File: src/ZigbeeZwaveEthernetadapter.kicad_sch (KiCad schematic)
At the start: 19 parts, among them J1 Barrel_Jack, J11 Conn_02x06_Odd_Even, J12 Conn_01x06, J14 Conn_01x06, J2 USB_B_Micro, J3 USB4125-GF-A, J31 Conn_02x05_Odd_Even, U1 TLV1117-33

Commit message: Add: BOM_A.pdf
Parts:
- J11: Manufacturer Part No. - -> RS2-12-G; Vendor - -> Digikey; Vendor Part No. - -> 2057-RS2-12-G-ND
- J12: Manufacturer Part No. - -> RS1-06-G; Vendor - -> Digikey; Vendor Part No. - -> 2057-RS1-06-G-ND
- J31: Manufacturer Part No. - -> RS2-10-G; Vendor - -> Digikey; Vendor Part No. - -> 2057-RS2-10-G-ND
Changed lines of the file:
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@@
       (effects (font (size 1.27 1.27)) hide)
     )
-    (property "Manufacturer Part No." "-" (at 62.23 48.26 0)
-      (effects (font (size 1.27 1.27)) hide)
-    )
-    (property "Vendor" "-" (at 62.23 48.26 0)
-      (effects (font (size 1.27 1.27)) hide)
-    )
-    (property "Vendor Part No." "-" (at 62.23 48.26 0)
+    (property "Manufacturer Part No." "RS2-12-G" (at 62.23 48.26 0)
+      (effects (font (size 1.27 1.27)) hide)
+    )
+    (property "Vendor" "Digikey" (at 62.23 48.26 0)
+      (effects (font (size 1.27 1.27)) hide)
+    )
+    (property "Vendor Part No." "2057-RS2-12-G-ND" (at 62.23 48.26 0)
       (effects (font (size 1.27 1.27)) hide)
     )
@@
       (effects (font (size 1.27 1.27)) hide)
     )
-    (property "Manufacturer Part No." "-" (at 151.13 63.5 0)
-      (effects (font (size 1.27 1.27)) hide)
-    )
-    (property "Vendor" "-" (at 151.13 63.5 0)
-      (effects (font (size 1.27 1.27)) hide)
-    )
-    (property "Vendor Part No." "-" (at 151.13 63.5 0)
+    (property "Manufacturer Part No." "RS2-10-G" (at 151.13 63.5 0)
+      (effects (font (size 1.27 1.27)) hide)
+    )
+    (property "Vendor" "Digikey" (at 151.13 63.5 0)
+      (effects (font (size 1.27 1.27)) hide)
+    )
+    (property "Vendor Part No." "2057-RS2-10-G-ND" (at 151.13 63.5 0)
       (effects (font (size 1.27 1.27)) hide)
     )
@@
       (effects (font (size 1.27 1.27)) hide)
     )
-    (property "Manufacturer Part No." "-" (at 52.07 93.98 0)
-      (effects (font (size 1.27 1.27)) hide)
-    )
-    (property "Vendor" "-" (at 52.07 93.98 0)
-      (effects (font (size 1.27 1.27)) hide)
-    )
-    (property "Vendor Part No." "-" (at 52.07 93.98 0)
-      (effects (font (size 1.27 1.27)) hide)
-    )
+    (property "Manufacturer Part No." "RS1-06-G" (at 52.07 93.98 0)
+      (effects (font (size 1.27 1.27)) hide)
+    )
+    (property "Vendor" "Digikey" (at 52.07 93.98 0)
+      (effects (font (size 1.27 1.27)) hide)
+    )
+    (property "Vendor Part No." "2057-RS1-06-G-ND" (at 52.07 93.98 0)
+      (effects (font (size 1.27 1.27)) hide)
+    )

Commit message: Mod: Schematic and PCB-Layout, finished new Version.
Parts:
- added H101, H102, H103, H104: MountingHole, MountingHole:MountingHole_2.7mm_M2.5_DIN965, symbol Mechanical:MountingHole
- added H105, H106, H107, H108: MountingHole, MountingHole:MountingHole_3.2mm_M3_DIN965, symbol Mechanical:MountingHole
- J14: Manufacturer Part No. - -> RS1-06-G; Vendor - -> Digikey; Vendor Part No. - -> 2057-RS1-06-G-ND
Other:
- note added: "Only one plug can be used at a time!"
- note added: "PCB Holes"
- note added: "WIZ Holes"
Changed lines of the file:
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@@
     (effects (font (size 1.27 1.27)) (justify right bottom))
+  )
+  (text "Only one plug can be used at a time!" (at 266.7 127 90)
+    (effects (font (size 2.54 2.54) (thickness 1.016) bold) (justify left bottom))
   )
   (text "WIZ ISP / Debug\nConnector" (at 49.53 76.2 0)
@@
   )
   (text "Raspberry Pi\nConnector" (at 139.7 38.1 0)
+    (effects (font (size 1.27 1.27) (thickness 0.254) bold) (justify left bottom))
+  )
+  (text "WIZ Holes" (at 49.53 172.72 0)
+    (effects (font (size 1.27 1.27) (thickness 0.254) bold) (justify left bottom))
+  )
+  (text "PCB Holes" (at 125.73 172.72 0)
     (effects (font (size 1.27 1.27) (thickness 0.254) bold) (justify left bottom))
   )
@@
     )
   )
+  (symbol (lib_id "Mechanical:MountingHole") (at 152.4 177.8 0) (unit 1)
+    (in_bom yes) (on_board yes) (dnp no) (fields_autoplaced)
+    (property "Reference" "H106" (at 154.94 176.53 0)
+      (effects (font (size 1.27 1.27)) (justify left))
+    )
+    (property "Value" "MountingHole" (at 154.94 179.07 0)
+      (effects (font (size 1.27 1.27)) (justify left))
+    )
+    (property "Footprint" "MountingHole:MountingHole_3.2mm_M3_DIN965" (at 152.4 177.8 0)
+      (effects (font (size 1.27 1.27)) hide)
+    )
+    (property "Datasheet" "~" (at 152.4 177.8 0)
+      (effects (font (size 1.27 1.27)) hide)
+    )
+    (instances
+      (project "ZigbeeZwaveEthernetadapter"
+        (path "/bfaac094-0365-40a4-8b7a-d4d62ace544e"
+          (reference "H106") (unit 1)
+        )
+      )
+    )
+  )
   (symbol (lib_id "Device:LED") (at 165.1 88.9 90) (unit 1)
     (in_bom yes) (on_board yes) (dnp no) (fields_autoplaced)
@@
     )
   )
+  (symbol (lib_id "Mechanical:MountingHole") (at 152.4 190.5 0) (unit 1)
+    (in_bom yes) (on_board yes) (dnp no) (fields_autoplaced)
+    (property "Reference" "H107" (at 154.94 189.23 0)
+      (effects (font (size 1.27 1.27)) (justify left))
+    )
+    (property "Value" "MountingHole" (at 154.94 191.77 0)
+      (effects (font (size 1.27 1.27)) (justify left))
+    )
+    (property "Footprint" "MountingHole:MountingHole_3.2mm_M3_DIN965" (at 152.4 190.5 0)
+      (effects (font (size 1.27 1.27)) hide)
+    )
+    (property "Datasheet" "~" (at 152.4 190.5 0)
+      (effects (font (size 1.27 1.27)) hide)
+    )
+    (instances
+      (project "ZigbeeZwaveEthernetadapter"
+        (path "/bfaac094-0365-40a4-8b7a-d4d62ace544e"
+          (reference "H107") (unit 1)
+        )
+      )
+    )
+  )
   (symbol (lib_id "power:+5V") (at 231.14 134.62 0) (unit 1)
     (in_bom yes) (on_board yes) (dnp no) (fields_autoplaced)
@@
       (effects (font (size 1.27 1.27)) hide)
     )
-    (property "Manufacturer Part No." "-" (at 52.07 144.78 0)
-      (effects (font (size 1.27 1.27)) hide)
-    )
-    (property "Vendor" "-" (at 52.07 144.78 0)
-      (effects (font (size 1.27 1.27)) hide)
-    )
-    (property "Vendor Part No." "-" (at 52.07 144.78 0)
+    (property "Manufacturer Part No." "RS1-06-G" (at 52.07 144.78 0)
+      (effects (font (size 1.27 1.27)) hide)
+    )
+    (property "Vendor" "Digikey" (at 52.07 144.78 0)
+      (effects (font (size 1.27 1.27)) hide)
+    )
+    (property "Vendor Part No." "2057-RS1-06-G-ND" (at 52.07 144.78 0)
       (effects (font (size 1.27 1.27)) hide)
     )
@@
     )
   )
+  (symbol (lib_id "Mechanical:MountingHole") (at 127 177.8 0) (unit 1)
+    (in_bom yes) (on_board yes) (dnp no) (fields_autoplaced)
+    (property "Reference" "H105" (at 129.54 176.53 0)
+      (effects (font (size 1.27 1.27)) (justify left))
+    )
+    (property "Value" "MountingHole" (at 129.54 179.07 0)
+      (effects (font (size 1.27 1.27)) (justify left))
+    )
+    (property "Footprint" "MountingHole:MountingHole_3.2mm_M3_DIN965" (at 127 177.8 0)
+      (effects (font (size 1.27 1.27)) hide)
+    )
+    (property "Datasheet" "~" (at 127 177.8 0)
+      (effects (font (size 1.27 1.27)) hide)
+    )
+    (instances
+      (project "ZigbeeZwaveEthernetadapter"
+        (path "/bfaac094-0365-40a4-8b7a-d4d62ace544e"
+          (reference "H105") (unit 1)
+        )
+      )
+    )
+  )
   (symbol (lib_id "power:+3V3") (at 63.5 86.36 0) (unit 1)
     (in_bom yes) (on_board yes) (dnp no) (fields_autoplaced)
@@
     )
   )
+  (symbol (lib_id "Mechanical:MountingHole") (at 127 190.5 0) (unit 1)
+    (in_bom yes) (on_board yes) (dnp no) (fields_autoplaced)
+    (property "Reference" "H108" (at 129.54 189.23 0)
+      (effects (font (size 1.27 1.27)) (justify left))
+    )
+    (property "Value" "MountingHole" (at 129.54 191.77 0)
+      (effects (font (size 1.27 1.27)) (justify left))
+    )
+    (property "Footprint" "MountingHole:MountingHole_3.2mm_M3_DIN965" (at 127 190.5 0)
+      (effects (font (size 1.27 1.27)) hide)
+    )
+    (property "Datasheet" "~" (at 127 190.5 0)
+      (effects (font (size 1.27 1.27)) hide)
+    )
+    (instances
+      (project "ZigbeeZwaveEthernetadapter"
+        (path "/bfaac094-0365-40a4-8b7a-d4d62ace544e"
+          (reference "H108") (unit 1)
+        )
+      )
+    )
+  )
   (symbol (lib_id "power:GND") (at 177.8 95.25 0) (unit 1)
     (in_bom yes) (on_board yes) (dnp no) (fields_autoplaced)
@@
         (path "/bfaac094-0365-40a4-8b7a-d4d62ace544e"
           (reference "#PWR0116") (unit 1)
+        )
+      )
+    )
+  )
+  (symbol (lib_id "Mechanical:MountingHole") (at 50.8 177.8 0) (unit 1)
+    (in_bom yes) (on_board yes) (dnp no) (fields_autoplaced)
+    (property "Reference" "H101" (at 53.34 176.53 0)
+      (effects (font (size 1.27 1.27)) (justify left))
+    )
+    (property "Value" "MountingHole" (at 53.34 179.07 0)
+      (effects (font (size 1.27 1.27)) (justify left))
+    )
+    (property "Footprint" "MountingHole:MountingHole_2.7mm_M2.5_DIN965" (at 50.8 177.8 0)
+      (effects (font (size 1.27 1.27)) hide)
+    )
+    (property "Datasheet" "~" (at 50.8 177.8 0)
+      (effects (font (size 1.27 1.27)) hide)
+    )
+    (instances
+      (project "ZigbeeZwaveEthernetadapter"
+        (path "/bfaac094-0365-40a4-8b7a-d4d62ace544e"
+          (reference "H101") (unit 1)
         )
       )
@@
     )
   )
+  (symbol (lib_id "Mechanical:MountingHole") (at 76.2 177.8 0) (unit 1)
+    (in_bom yes) (on_board yes) (dnp no) (fields_autoplaced)
+    (property "Reference" "H102" (at 78.74 176.53 0)
+      (effects (font (size 1.27 1.27)) (justify left))
+    )
+    (property "Value" "MountingHole" (at 78.74 179.07 0)
+      (effects (font (size 1.27 1.27)) (justify left))
+    )
+    (property "Footprint" "MountingHole:MountingHole_2.7mm_M2.5_DIN965" (at 76.2 177.8 0)
+      (effects (font (size 1.27 1.27)) hide)
+    )
+    (property "Datasheet" "~" (at 76.2 177.8 0)
+      (effects (font (size 1.27 1.27)) hide)
+    )
+    (instances
+      (project "ZigbeeZwaveEthernetadapter"
+        (path "/bfaac094-0365-40a4-8b7a-d4d62ace544e"
+          (reference "H102") (unit 1)
+        )
+      )
+    )
+  )
   (symbol (lib_id "Connector:USB_B_Micro") (at 241.3 101.6 0) (mirror y) (unit 1)
     (in_bom yes) (on_board yes) (dnp no)
@@
         (path "/bfaac094-0365-40a4-8b7a-d4d62ace544e"
           (reference "#PWR0123") (unit 1)
+        )
+      )
+    )
+  )
+  (symbol (lib_id "Mechanical:MountingHole") (at 76.2 190.5 0) (unit 1)
+    (in_bom yes) (on_board yes) (dnp no) (fields_autoplaced)
+    (property "Reference" "H103" (at 78.74 189.23 0)
+      (effects (font (size 1.27 1.27)) (justify left))
+    )
+    (property "Value" "MountingHole" (at 78.74 191.77 0)
+      (effects (font (size 1.27 1.27)) (justify left))
+    )
+    (property "Footprint" "MountingHole:MountingHole_2.7mm_M2.5_DIN965" (at 76.2 190.5 0)
+      (effects (font (size 1.27 1.27)) hide)
+    )
+    (property "Datasheet" "~" (at 76.2 190.5 0)
+      (effects (font (size 1.27 1.27)) hide)
+    )
+    (instances
+      (project "ZigbeeZwaveEthernetadapter"
+        (path "/bfaac094-0365-40a4-8b7a-d4d62ace544e"
+          (reference "H103") (unit 1)
         )
       )
@@
         )
       )
+    )
+  )
+  (symbol (lib_id "Mechanical:MountingHole") (at 50.8 190.5 0) (unit 1)
+    (in_bom yes) (on_board yes) (dnp no) (fields_autoplaced)
+    (property "Reference" "H104" (at 53.34 189.23 0)
+      (effects (font (size 1.27 1.27)) (justify left))
+    )
+    (property "Value" "MountingHole" (at 53.34 191.77 0)
+      (effects (font (size 1.27 1.27)) (justify left))
+    )
+    (property "Footprint" "MountingHole:MountingHole_2.7mm_M2.5_DIN965" (at 50.8 190.5 0)
+      (effects (font (size 1.27 1.27)) hide)
+    )
+    (property "Datasheet" "~" (at 50.8 190.5 0)
+      (effects (font (size 1.27 1.27)) hide)
+    )
+    (instances
+      (project "ZigbeeZwaveEthernetadapter"
+        (path "/bfaac094-0365-40a4-8b7a-d4d62ace544e"
+          (reference "H104") (unit 1)
+        )
+      )

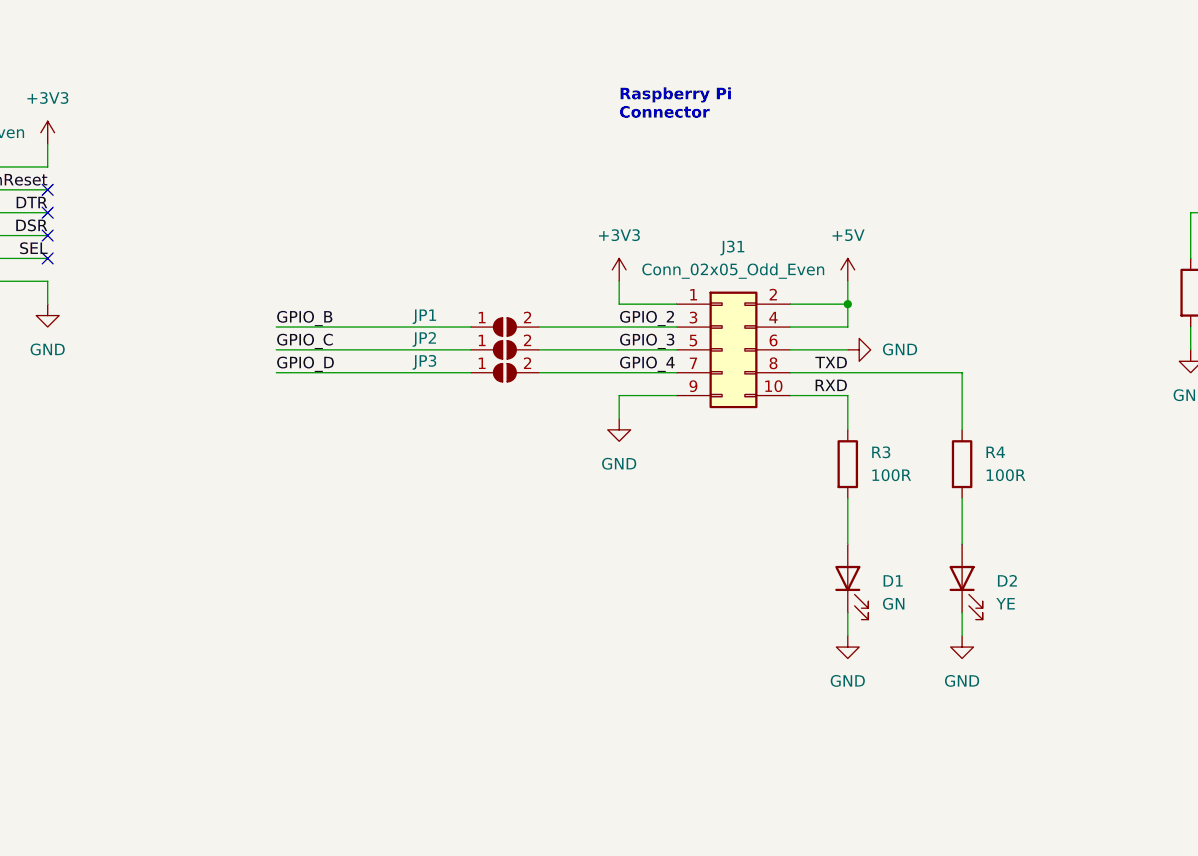
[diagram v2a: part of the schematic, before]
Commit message: Mod: LEDs for RXD and TXD, changed from Pull-Down to Pull-Up resistors and changed their value. Re-exported all the files.
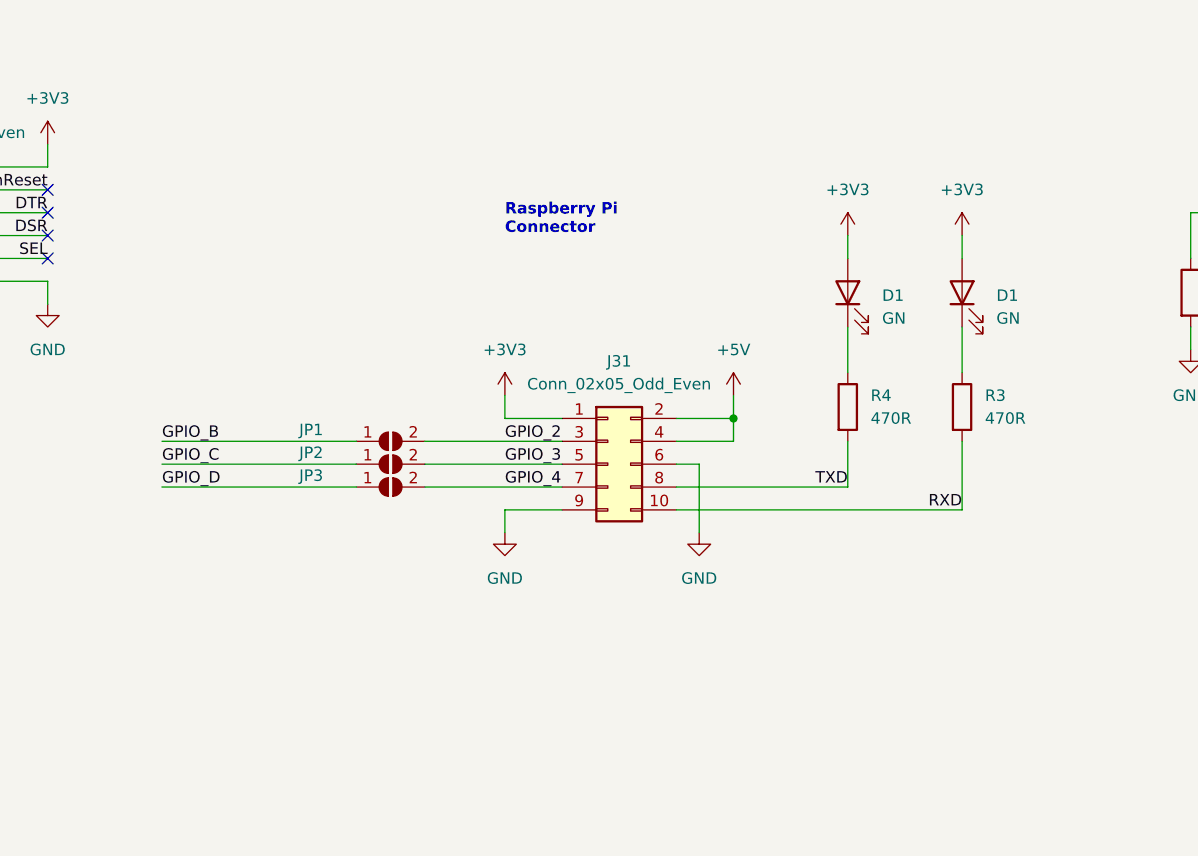
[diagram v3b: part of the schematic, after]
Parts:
- removed D2: YE, LED_SMD:LED_0805_2012Metric_Pad1.15x1.40mm_HandSolder, symbol Device:LED
- added D1: GN, LED_SMD:LED_0805_2012Metric_Pad1.15x1.40mm_HandSolder, symbol Device:LED
- J1: footprint Connector_User:CUI_PJ-037A -> Connector_User:CUI_PJ-037A_Board-Edge
- R3, R4: value 100R -> 470R; Manufacturer Part No. RC0805FR-07100RL -> RC0805FR-07470RL; Vendor Part No. 311-100CRCT-ND -> 311-470CRCT-ND
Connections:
- net +3V3: now also D1.2 (A), D1.2 (A)
- net GND: no longer D1.1 (K)
- net RXD: now also R3.2; no longer R3.1
- net TXD: now also R4.2; no longer R4.1
- new net: D1.1 (K), R3.1
- new net: D1.1 (K), R4.1
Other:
- moved on the sheet: D1, J31, JP1, JP2, JP3, R3, R4

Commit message: Mod: Updated project to KiCad 8.0
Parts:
- J106: renamed from J3; footprint Connector_User:GCT_USB4125-GF-A -> Connectors_User:GCT_USB4125-GF-A
- renumbered C1 to C101, C2 to C102, D1 to D101, D1 to D102, J11 to J101, J12 to J102, J14 to J104, J31 to J105, J2 to J107, J1 to J108, JP1 to JP101, JP2 to JP102, JP3 to JP103, R1 to R101, R2 to R102, R4 to R103, R3 to R104, U1 to U101

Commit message: Mod: ZigbeeZwaveEthernetadapter.kicad_sch, changes part no. of C101
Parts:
- C101: Manufacturer Part No. TLJP107M006R5400 -> CL21A107MQYNNWE; Vendor Part No. 478-5260-1-ND -> 1276-CL21A107MQYNNWECT-ND
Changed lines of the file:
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@@
 			)
 		)
-		(property "Manufacturer Part No." "TLJP107M006R5400"
+		(property "Manufacturer Part No." "CL21A107MQYNNWE"
 			(at 127 146.05 0)
 			(effects
@@
 			)
 		)
-		(property "Vendor Part No." "478-5260-1-ND"
+		(property "Vendor Part No." "1276-CL21A107MQYNNWECT-ND"
 			(at 127 146.05 0)
 			(effects
